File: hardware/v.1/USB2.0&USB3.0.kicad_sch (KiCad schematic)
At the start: 20 parts, among them J4 USB3_A_Stacked, J5 USB_A_Stacked, U3 ULC0524P, U4 ULC0524P, U5 ULC0524P

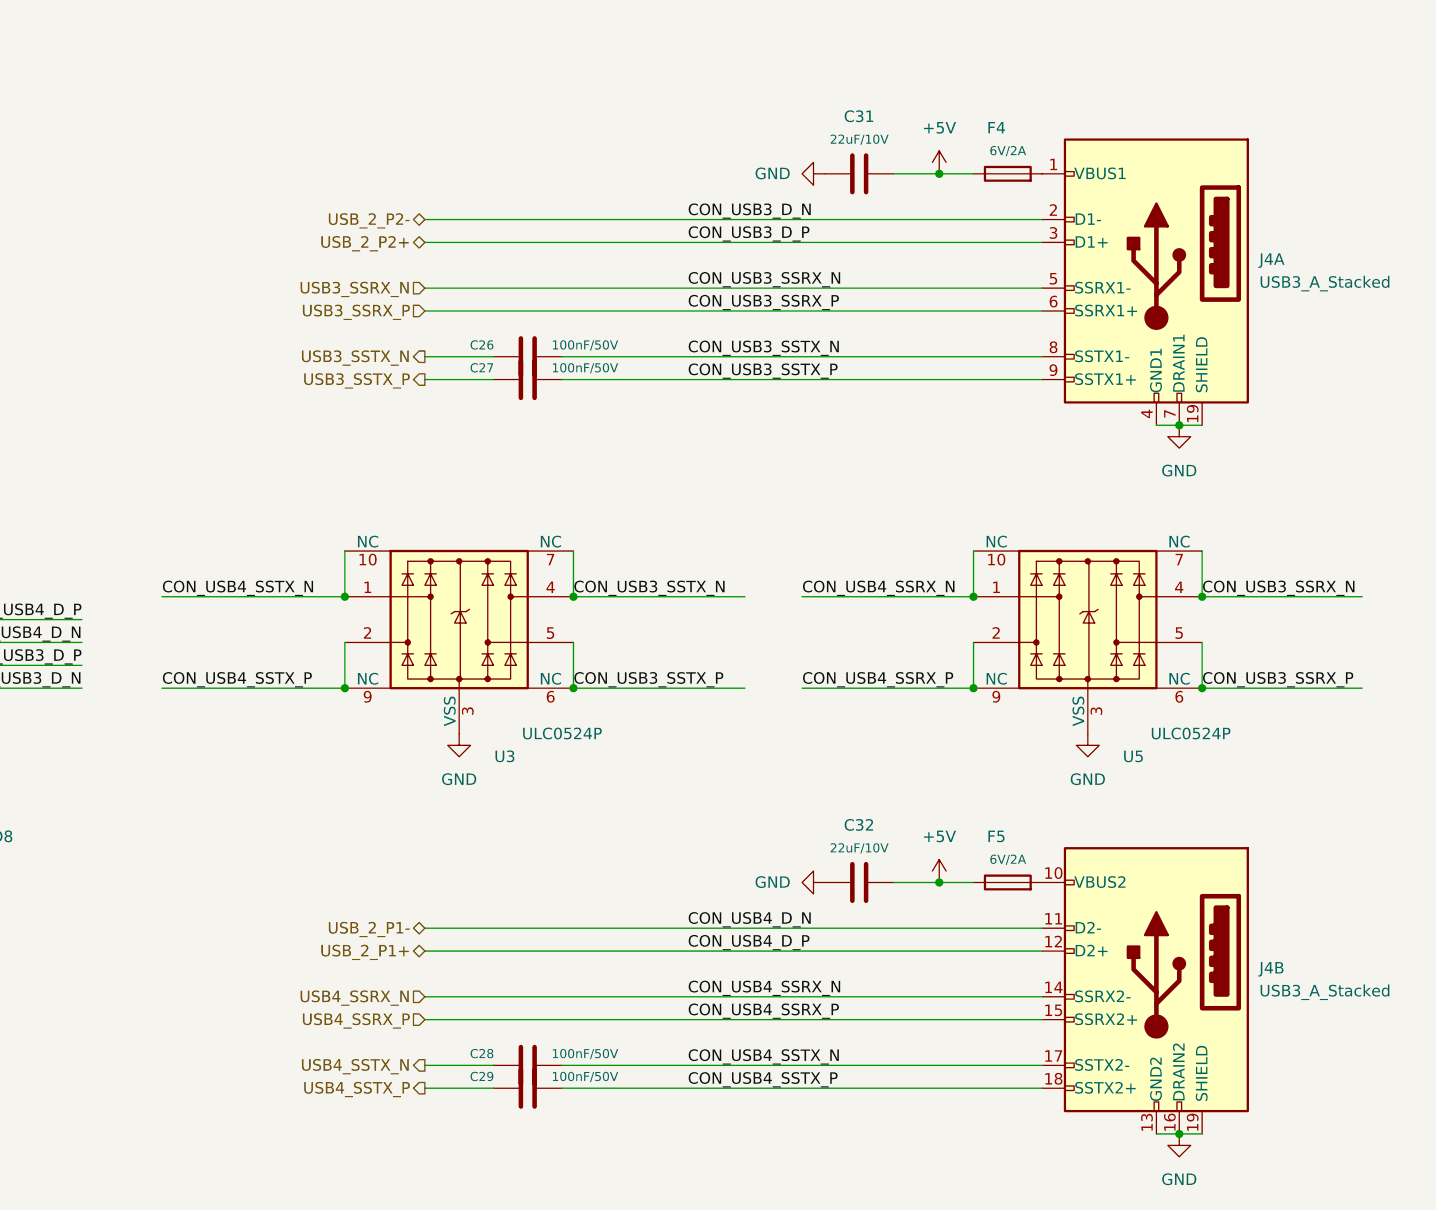
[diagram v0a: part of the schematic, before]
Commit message: finish the back IO, roughly establish HSIO placement
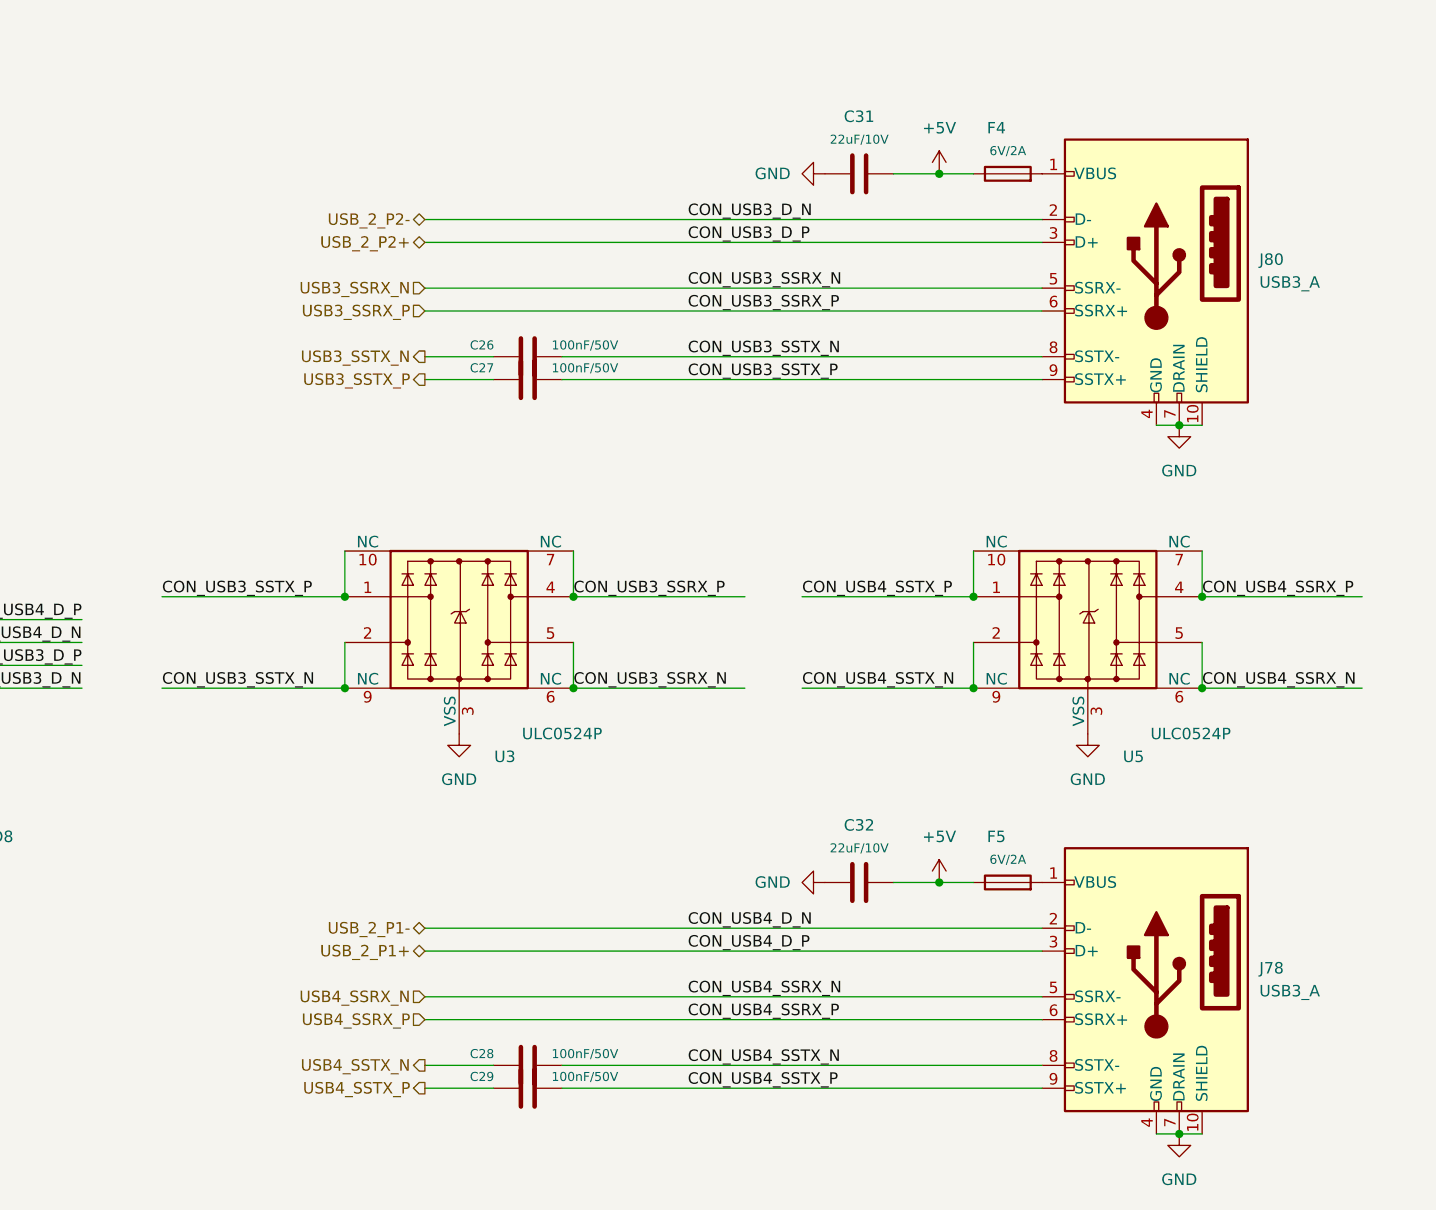
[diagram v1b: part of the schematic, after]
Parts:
- removed J4: USB3_A_Stacked, A_HDJ_Library:USB3_A_Molex_48406-0001_Horizontal_Stacked, symbol Connector:USB3_A_Stacked
- added J78, J80: USB3_A, Connector_USB:USB3_A_Receptacle_Wuerth_692122030100, symbol Connector:USB3_A
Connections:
- net CON_USB3_SSTX_N: now also U3.2, U3.9 (NC), J80.8 (SSTX-); no longer U3.4, U3.7 (NC)
- net CON_USB3_SSTX_P: now also U3.1, U3.10 (NC), J80.9 (SSTX+); no longer U3.5, U3.6 (NC)
- net CON_USB4_SSTX_N: now also U5.2, U5.9 (NC), J78.8 (SSTX-); no longer U3.1, U3.10 (NC)
- net CON_USB4_SSTX_P: now also U5.1, U5.10 (NC), J78.9 (SSTX+); no longer U3.2, U3.9 (NC)
- net GND: now also J78.10 (SHIELD), J78.4 (GND), J78.7 (DRAIN), J80.10 (SHIELD), J80.4 (GND), J80.7 (DRAIN)
- net USB3_SSRX_N: now also U3.5, U3.6 (NC), J80.5 (SSRX-); no longer U5.4, U5.7 (NC)
- net USB3_SSRX_P: now also U3.4, U3.7 (NC), J80.6 (SSRX+); no longer U5.5, U5.6 (NC)
- net USB4_SSRX_N: now also U5.5, U5.6 (NC), J78.5 (SSRX-); no longer U5.1, U5.10 (NC)
- net USB4_SSRX_P: now also U5.4, U5.7 (NC), J78.6 (SSRX+); no longer U5.2, U5.9 (NC)
- net USB_2_P1+: now also J78.3 (D+)
- net USB_2_P1-: now also J78.2 (D-)
- net USB_2_P2+: now also J80.3 (D+)
- net USB_2_P2-: now also J80.2 (D-)
- net at F4.2: now also J80.1 (VBUS)
- net at F5.2: now also J78.1 (VBUS)
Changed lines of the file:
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@@
 		)
 	)
-	(label "CON_USB3_SSTX_N"
+	(label "CON_USB3_SSRX_P"
 		(at 261.62 228.6 0)
 		(effects
@@
 		)
 	)
-	(label "CON_USB3_SSTX_P"
+	(label "CON_USB3_SSRX_N"
 		(at 261.62 238.76 0)
 		(effects
@@
 		)
 	)
-	(label "CON_USB4_SSTX_P"
+	(label "CON_USB3_SSTX_N"
 		(at 215.9 238.76 0)
 		(effects
@@
 		)
 	)
-	(label "CON_USB3_SSRX_N"
+	(label "CON_USB4_SSRX_P"
 		(at 331.47 228.6 0)
 		(effects
@@
 		)
 	)
-	(label "CON_USB4_SSRX_N"
+	(label "CON_USB4_SSTX_P"
 		(at 287.02 228.6 0)
 		(effects
@@
 		)
 	)
-	(label "CON_USB4_SSTX_N"
+	(label "CON_USB3_SSTX_P"
 		(at 215.9 228.6 0)
 		(effects
@@
 		)
 	)
-	(label "CON_USB4_SSRX_P"
+	(label "CON_USB4_SSTX_N"
 		(at 287.02 238.76 0)
 		(effects
@@
 		)
 	)
-	(label "CON_USB3_SSRX_P"
+	(label "CON_USB4_SSRX_N"
 		(at 331.47 238.76 0)
 		(effects
@@
 	)
 	(symbol
-		(lib_id "Connector:USB3_A_Stacked")
-		(at 326.39 191.77 0)
-		(mirror y)
-		(unit 1)
-		(exclude_from_sim no)
-		(in_bom yes)
-		(on_board yes)
-		(dnp no)
-		(fields_autoplaced yes)
-		(property "Reference" "J4"
-			(at 337.82 191.135 0)
-			(effects
-				(font
-					(size 1.27 1.27)
-				)
-				(justify right)
-			)
-		)
-		(property "Value" "USB3_A_Stacked"
-			(at 337.82 193.675 0)
-			(effects
-				(font
-					(size 1.27 1.27)
-				)
-				(justify right)
-			)
-		)
-		(property "Footprint" "A_HDJ_Library:USB3_A_Molex_48406-0001_Horizontal_Stacked"
-			(at 322.58 189.23 0)
-			(effects
-				(font
-					(size 1.27 1.27)
-				)
-				(hide yes)
-			)
-		)
-		(property "Datasheet" "~"
-			(at 322.58 189.23 0)
-			(effects
-				(font
-					(size 1.27 1.27)
-				)
-				(hide yes)
-			)
-		)
-		(property "Description" ""
-			(at 326.39 191.77 0)
-			(effects
-				(font
-					(size 1.27 1.27)
-				)
-				(hide yes)
-			)
-		)
-		(property "SCH_Show_Footprint" ""
-			(at 326.39 191.77 0)
-			(effects
-				(font
-					(size 1.27 1.27)
-				)
-				(hide yes)
-			)
-		)
-		(property "Sim.Device" ""
-			(at 326.39 191.77 0)
-			(effects
-				(font
-					(size 1.27 1.27)
-				)
-				(hide yes)
-			)
-		)
-		(property "Sim.Pins" ""
-			(at 326.39 191.77 0)
-			(effects
-				(font
-					(size 1.27 1.27)
-				)
-				(hide yes)
-			)
-		)
-		(property "Sim.Type" ""
-			(at 326.39 191.77 0)
-			(effects
-				(font
-					(size 1.27 1.27)
-				)
-				(hide yes)
-			)
-		)
-		(pin "3"
-		)
-		(pin "15"
-		)
-		(pin "2"
-		)
-		(pin "12"
-		)
-		(pin "13"
-		)
-		(pin "9"
-		)
-		(pin "17"
-		)
-		(pin "6"
-		)
-		(pin "14"
-		)
-		(pin "11"
-		)
-		(pin "10"
-		)
-		(pin "1"
-		)
-		(pin "5"
-		)
-		(pin "7"
-		)
-		(pin "8"
-		)
-		(pin "16"
-		)
-		(pin "4"
-		)
-		(pin "19"
-		)
-		(pin "18"
-		)
-		(instances
-			(project "[DFR1142]Lite Carrier for LattePanda Mu"
-				(path "/2a6d114a-7fd7-4207-b5f7-4ea9c34f36aa/f9aa04f2-8362-4e9f-9e54-e2b1a8ec9b0a"
-					(reference "J4")
-					(unit 1)
-				)
-			)
-		)
-	)
-	(symbol
 		(lib_id "Power_Protection:D3V3XA4B10LP")
 		(at 287.02 129.54 0)
@@
 				(path "/2a6d114a-7fd7-4207-b5f7-4ea9c34f36aa/f9aa04f2-8362-4e9f-9e54-e2b1a8ec9b0a"
 					(reference "U5")
+					(unit 1)
+				)
+			)
+		)
+	)
+	(symbol
+		(lib_id "Connector:USB3_A")
+		(at 326.39 270.51 0)
+		(mirror y)
+		(unit 1)
+		(exclude_from_sim no)
+		(in_bom yes)
+		(on_board yes)
+		(dnp no)
+		(fields_autoplaced yes)
+		(property "Reference" "J78"
+			(at 337.82 269.8749 0)
+			(effects
+				(font
+					(size 1.27 1.27)
+				)
+				(justify right)
+			)
+		)
+		(property "Value" "USB3_A"
+			(at 337.82 272.4149 0)
+			(effects
+				(font
+					(size 1.27 1.27)
+				)
+				(justify right)
+			)
+		)
+		(property "Footprint" "Connector_USB:USB3_A_Receptacle_Wuerth_692122030100"
+			(at 322.58 267.97 0)
+			(effects
+				(font
+					(size 1.27 1.27)
+				)
+				(hide yes)
+			)
+		)
+		(property "Datasheet" "~"
+			(at 322.58 267.97 0)
+			(effects
+				(font
+					(size 1.27 1.27)
+				)
+				(hide yes)
+			)
+		)
+		(property "Description" "USB 3.0 A connector"
+			(at 326.39 270.51 0)
+			(effects
+				(font
+					(size 1.27 1.27)
+				)
+				(hide yes)
+			)
+		)
+		(pin "5"
+		)
+		(pin "10"
+		)
+		(pin "2"
+		)
+		(pin "8"
+		)
+		(pin "1"
+		)
+		(pin "3"
+		)
+		(pin "7"
+		)
+		(pin "4"
+		)
+		(pin "9"
+		)
+		(pin "6"
+		)
+		(instances
+			(project "[DFR1142]Lite Carrier for LattePanda Mu"
+				(path "/2a6d114a-7fd7-4207-b5f7-4ea9c34f36aa/f9aa04f2-8362-4e9f-9e54-e2b1a8ec9b0a"
+					(reference "J78")
 					(unit 1)
 				)
@@
 	)
 	(symbol
-		(lib_id "Connector:USB3_A_Stacked")
-		(at 326.39 270.51 0)
+		(lib_id "Connector:USB3_A")
+		(at 326.39 191.77 0)
 		(mirror y)
-		(unit 2)
+		(unit 1)
 		(exclude_from_sim no)
 		(in_bom yes)
@@
 		(dnp no)
 		(fields_autoplaced yes)
-		(property "Reference" "J4"
-			(at 337.82 269.875 0)
+		(property "Reference" "J80"
+			(at 337.82 191.1349 0)
 			(effects
 				(font
@@
 			)
 		)
-		(property "Value" "USB3_A_Stacked"
-			(at 337.82 272.415 0)
+		(property "Value" "USB3_A"
+			(at 337.82 193.6749 0)
 			(effects
 				(font
@@
 			)
 		)
-		(property "Footprint" "A_HDJ_Library:USB3_A_Molex_48406-0001_Horizontal_Stacked"
-			(at 322.58 267.97 0)
+		(property "Footprint" "Connector_USB:USB3_A_Receptacle_Wuerth_692122030100"
+			(at 322.58 189.23 0)
 			(effects
 				(font
@@
 		)
 		(property "Datasheet" "~"
-			(at 322.58 267.97 0)
-			(effects
-				(font
-					(size 1.27 1.27)
-				)
-				(hide yes)
-			)
-		)
-		(property "Description" ""
-			(at 326.39 270.51 0)
-			(effects
-				(font
-					(size 1.27 1.27)
-				)
-				(hide yes)
-			)
-		)
-		(property "SCH_Show_Footprint" ""
-			(at 326.39 270.51 0)
-			(effects
-				(font
-					(size 1.27 1.27)
-				)
-				(hide yes)
-			)
-		)
-		(property "Sim.Device" ""
-			(at 326.39 270.51 0)
-			(effects
-				(font
-					(size 1.27 1.27)
-				)
-				(hide yes)
-			)
-		)
-		(property "Sim.Pins" ""
-			(at 326.39 270.51 0)
-			(effects
-				(font
-					(size 1.27 1.27)
-				)
-				(hide yes)
-			)
-		)
-		(property "Sim.Type" ""
-			(at 326.39 270.51 0)
-			(effects
-				(font
-					(size 1.27 1.27)
-				)
-				(hide yes)
-			)
+			(at 322.58 189.23 0)
+			(effects
+				(font
+					(size 1.27 1.27)
+				)
+				(hide yes)
+			)
+		)
+		(property "Description" "USB 3.0 A connector"
+			(at 326.39 191.77 0)
+			(effects
+				(font
+					(size 1.27 1.27)
+				)
+				(hide yes)
+			)
+		)
+		(pin "5"
+		)
+		(pin "10"
+		)
+		(pin "2"
+		)
+		(pin "8"
+		)
+		(pin "1"
+		)
+		(pin "3"
+		)
+		(pin "7"
+		)
+		(pin "4"
+		)
+		(pin "9"
 		)
 		(pin "6"
 		)
-		(pin "17"
-		)
-		(pin "12"
-		)
-		(pin "14"
-		)
-		(pin "2"
-		)
-		(pin "16"
-		)
-		(pin "7"
-		)
-		(pin "9"
-		)
-		(pin "3"
-		)
-		(pin "11"
-		)
-		(pin "13"
-		)
-		(pin "19"
-		)
-		(pin "5"
-		)
-		(pin "18"
-		)
-		(pin "4"
-		)
-		(pin "1"
-		)
-		(pin "8"
-		)
-		(pin "10"
-		)
-		(pin "15"
-		)
 		(instances
-			(project "[DFR1142]Lite Carrier for LattePanda Mu"
+			(project ""
 				(path "/2a6d114a-7fd7-4207-b5f7-4ea9c34f36aa/f9aa04f2-8362-4e9f-9e54-e2b1a8ec9b0a"
-					(reference "J4")
-					(unit 2)
+					(reference "J80")
+					(unit 1)
 				)
 			)
@@
 		(exclude_from_sim no)
 		(in_bom yes)
-		(on_board yes)
+		(on_board no)
 		(dnp no)
 		(fields_autoplaced yes)
